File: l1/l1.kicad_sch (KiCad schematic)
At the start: 0 parts

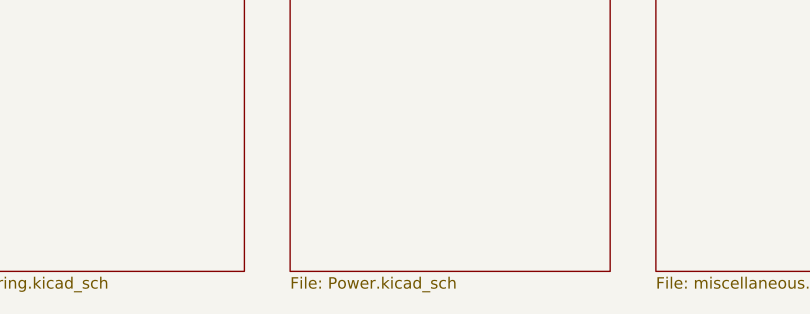
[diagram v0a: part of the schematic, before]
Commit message: Changed To G071
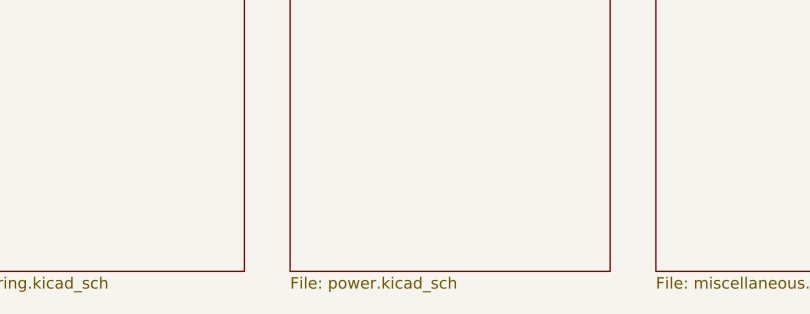
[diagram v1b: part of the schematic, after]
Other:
- sheet Power: file Power.kicad_sch -> power.kicad_sch

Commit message: rough ideation
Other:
- removed sheet Boost Switch
- removed sheet Motor Driver
- removed sheet Power
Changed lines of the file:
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@@
-	)
-	(sheet
-		(at 30.48 88.9)
-		(size 35.56 33.02)
-		(fields_autoplaced yes)
-		(stroke
-			(width 0.1524)
-			(type solid)
-		)
-		(fill
-			(color 0 0 0 0.0000)
-		)
-		(property "Sheetname" "Motor Driver"
-			(at 30.48 88.1884 0)
-			(effects
-				(font
-					(size 1.27 1.27)
-				)
-				(justify left bottom)
-			)
-		)
-		(property "Sheetfile" "motordriver.kicad_sch"
-			(at 30.48 122.5046 0)
-			(effects
-				(font
-					(size 1.27 1.27)
-				)
-				(justify left top)
-			)
-		)
-		(instances
-			(project "l1"
-				(path "/0e4ddce5-5c0a-41d1-ab67-e7bad6d98362"
-					(page "10")
-				)
-			)
-		)
-	)
-	(sheet
-		(at 195.58 88.9)
-		(size 35.56 33.02)
-		(fields_autoplaced yes)
-		(stroke
-			(width 0.1524)
-			(type solid)
-		)
-		(fill
-			(color 0 0 0 0.0000)
-		)
-		(property "Sheetname" "Power"
-			(at 195.58 88.1884 0)
-			(effects
-				(font
-					(size 1.27 1.27)
-				)
-				(justify left bottom)
-			)
-		)
-		(property "Sheetfile" "power.kicad_sch"
-			(at 195.58 122.5046 0)
-			(effects
-				(font
-					(size 1.27 1.27)
-				)
-				(justify left top)
-			)
-		)
-		(instances
-			(project "l1"
-				(path "/0e4ddce5-5c0a-41d1-ab67-e7bad6d98362"
-					(page "5")
-				)
-			)
-		)
 	)
 	(sheet
@@
 				)
 			)
-		)
-	)
-	(sheet
-		(at 115.57 88.9)
-		(size 34.29 33.02)
-		(fields_autoplaced yes)
-		(stroke
-			(width 0.1524)
-			(type solid)
-		)
-		(fill
-			(color 0 0 0 0.0000)
-		)
-		(property "Sheetname" "Boost Switch"
-			(at 115.57 88.1884 0)
-			(effects
-				(font
-					(size 1.27 1.27)
-				)
-				(justify left bottom)
-			)
-		)
-		(property "Sheetfile" "boost-switch.kicad_sch"
-			(at 115.57 122.5046 0)
-			(effects
-				(font
-					(size 1.27 1.27)
-				)
-				(justify left top)
-			)
-		)
-		(instances
-			(project "l1"
-				(path "/0e4ddce5-5c0a-41d1-ab67-e7bad6d98362"
-					(page "9")
-				)
-			)

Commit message: gate
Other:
- added sheet Gate (Gate.kicad_sch)
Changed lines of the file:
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@@
 	)
 	(sheet
-		(at 73.66 88.9)
+		(at 71.12 88.9)
+		(size 34.29 33.02)
+		(fields_autoplaced yes)
+		(stroke
+			(width 0.1524)
+			(type solid)
+		)
+		(fill
+			(color 0 0 0 0.0000)
+		)
+		(property "Sheetname" "Gate"
+			(at 71.12 88.1884 0)
+			(effects
+				(font
+					(size 1.27 1.27)
+				)
+				(justify left bottom)
+			)
+		)
+		(property "Sheetfile" "Gate.kicad_sch"
+			(at 71.12 122.5046 0)
+			(effects
+				(font
+					(size 1.27 1.27)
+				)
+				(justify left top)
+			)
+		)
+		(instances
+			(project "l1"
+				(path "/0e4ddce5-5c0a-41d1-ab67-e7bad6d98362"
+					(page "8")
+				)
+			)
+		)
+	)
+	(sheet
+		(at 21.59 88.9)
 		(size 35.56 33.02)
 		(fields_autoplaced yes)
@@
 		)
 		(property "Sheetname" "Connections"
-			(at 73.66 88.1884 0)
+			(at 21.59 88.1884 0)
 			(effects
 				(font
@@
 		)
 		(property "Sheetfile" "connections.kicad_sch"
-			(at 73.66 122.5046 0)
+			(at 21.59 122.5046 0)
 			(effects
 				(font
